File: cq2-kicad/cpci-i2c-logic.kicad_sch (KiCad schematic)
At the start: 25 parts, among them SW1 1.27 pitch, U10 PCA9546A, U11 24LC02B, U12 74LVC2G125, U9 PCA9554A

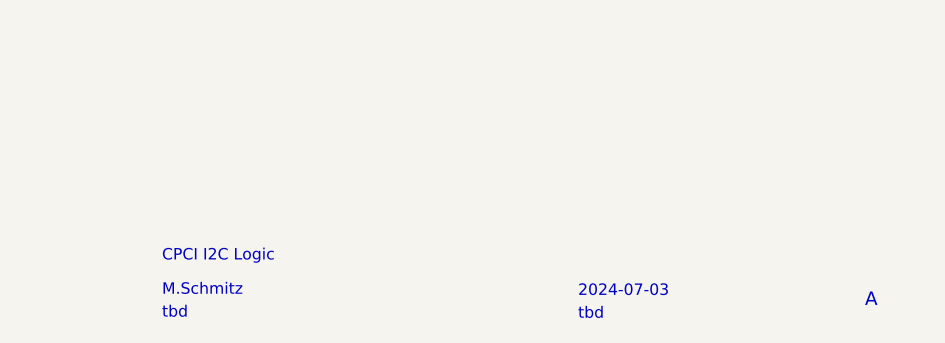
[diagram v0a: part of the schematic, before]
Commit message: drc checked before panalization
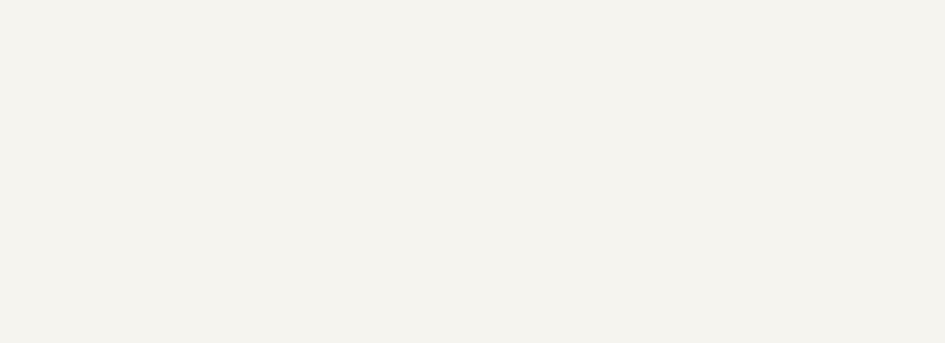
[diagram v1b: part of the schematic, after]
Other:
- note removed: "2024-07-03"
- note removed: "A"
- note removed: "CPCI I2C Logic"
- note removed: "M.Schmitz"
- note removed: "tbd"
- title: (none) -> CQ2
